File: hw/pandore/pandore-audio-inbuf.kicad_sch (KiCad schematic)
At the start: 29 parts, among them U17 OPAMP_DIFF_1

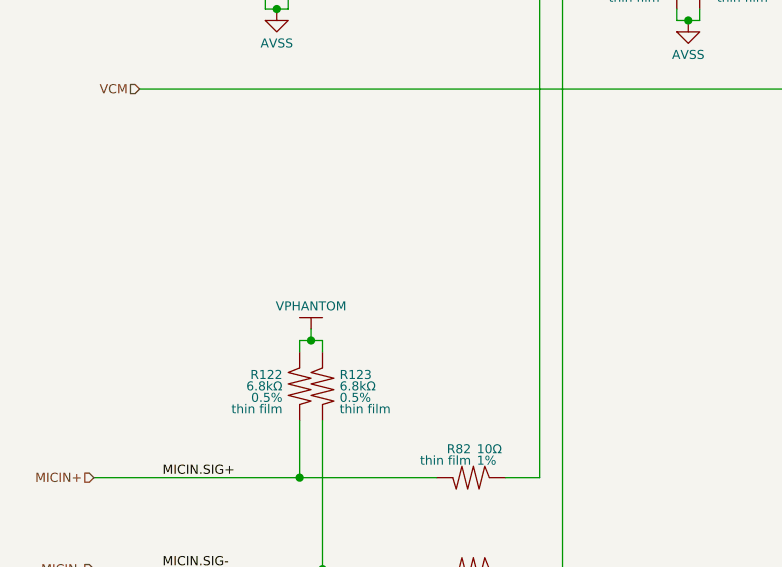
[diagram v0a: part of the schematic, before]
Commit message: Lots of routing done power blocks intra-routing mostly done rp2350 routing mostly done some label cleanup
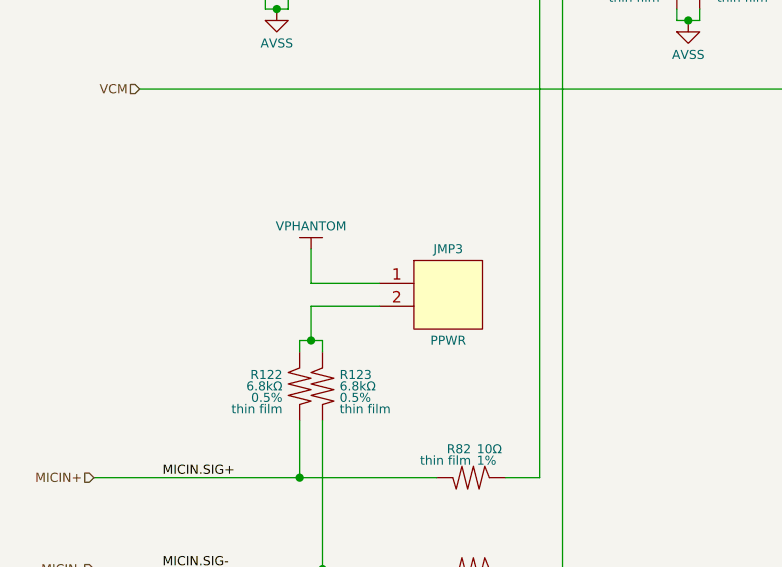
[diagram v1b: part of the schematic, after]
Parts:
- added JMP3: PPWR, reekilib_con:HDR254P1X02-TH, symbol reekilib_con:hdr-1x2
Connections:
- net VPHANTOM: now also JMP3.1; no longer R122.2, R123.2
- new net: JMP3.2, R122.2, R123.2
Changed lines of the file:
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@@
 	(wire
 		(pts
-			(xy 86.36 107.95) (xy 86.36 109.22)
-		)
-		(stroke
-			(width 0)
-			(type default)
-		)
-	)
-	(wire
-		(pts
 			(xy 156.21 77.47) (xy 156.21 62.23)
 		)
@@
 	(wire
 		(pts
+			(xy 93.98 105.41) (xy 86.36 105.41)
+		)
+		(stroke
+			(width 0)
+			(type default)
+		)
+	)
+	(wire
+		(pts
 			(xy 190.5 81.28) (xy 190.5 82.55)
 		)
@@
 	(wire
 		(pts
+			(xy 86.36 99.06) (xy 86.36 102.87)
+		)
+		(stroke
+			(width 0)
+			(type default)
+		)
+	)
+	(wire
+		(pts
 			(xy 193.04 45.72) (xy 193.04 52.07)
 		)
@@
 	(wire
 		(pts
+			(xy 86.36 102.87) (xy 93.98 102.87)
+		)
+		(stroke
+			(width 0)
+			(type default)
+		)
+	)
+	(wire
+		(pts
+			(xy 86.36 105.41) (xy 86.36 109.22)
+		)
+		(stroke
+			(width 0)
+			(type default)
+		)
+	)
+	(wire
+		(pts
 			(xy 190.5 175.26) (xy 191.77 175.26)
 		)
@@
 		)
 	)
+	(netclass_flag ""
+		(length 1.27)
+		(shape diamond)
+		(at 87.63 105.41 0)
+		(fields_autoplaced yes)
+		(effects
+			(font
+				(size 1.016 1.016)
+			)
+			(justify left bottom)
+		)
+		(property "Netclass" "PWR"
+			(at 88.7273 104.14 0)
+			(effects
+				(font
+					(size 1.27 1.27)
+				)
+				(justify left)
+			)
+		)
+		(property "Component Class" ""
+			(at -86.36 68.58 0)
+			(effects
+				(font
+					(size 1.27 1.27)
+					(italic yes)
+				)
+			)
+		)
+	)
 	(symbol
 		(lib_id "reekilib_cap:cap")
@@
 	)
 	(symbol
+		(lib_id "reekilib_con:hdr-1x2")
+		(at 101.6 104.14 0)
+		(unit 1)
+		(exclude_from_sim yes)
+		(in_bom yes)
+		(on_board yes)
+		(dnp no)
+		(fields_autoplaced yes)
+		(property "Reference" "JMP3"
+			(at 101.6 99.06 0)
+			(do_not_autoplace yes)
+			(effects
+				(font
+					(size 1 1)
+				)
+			)
+		)
+		(property "Value" "PPWR"
+			(at 101.6 109.22 0)
+			(do_not_autoplace yes)
+			(effects
+				(font
+					(size 1 1)
+				)
+			)
+		)
+		(property "Footprint" "reekilib_con:HDR254P1X02-TH"
+			(at 101.6 112.268 0)
+			(do_not_autoplace yes)
+			(effects
+				(font
+					(size 1 1)
+				)
+				(hide yes)
+			)
+		)
+		(property "Datasheet" "url-ds"
+			(at 101.6 116.586 0)
+			(do_not_autoplace yes)
+			(effects
+				(font
+					(size 1 1)
+				)
+				(hide yes)
+			)
+		)
+		(property "Description" "header 1row 2pin"
+			(at 101.6 113.792 0)
+			(do_not_autoplace yes)
+			(effects
+				(font
+					(size 1 1)
+				)
+				(hide yes)
+			)
+		)
+		(property "MPN" "MPN"
+			(at 101.6 110.744 0)
+			(do_not_autoplace yes)
+			(effects
+				(font
+					(size 1 1)
+				)
+				(hide yes)
+			)
+		)
+		(property "MFG" "MFG"
+			(at 108.204 110.744 0)
+			(do_not_autoplace yes)
+			(effects
+				(font
+					(size 1 1)
+				)
+				(justify left)
+				(hide yes)
+			)
+		)
+		(property "Link" "url-link"
+			(at 101.6 115.316 0)
+			(do_not_autoplace yes)
+			(effects
+				(font
+					(size 1 1)
+				)
+				(hide yes)
+			)
+		)
+		(pin "2"
+		)
+		(pin "1"
+		)
+		(instances
+			(project ""
+				(path "/e55f2700-f75a-4062-8a27-fe258faa8966/b4e2772d-7748-46ec-bd38-bc8e72cebcb8/505def28-a163-4964-82bd-abe7e8697de4/8d59667e-74a9-4b74-9da4-c408ef8d4019"
+					(reference "JMP3")
+					(unit 1)
+				)
+				(path "/e55f2700-f75a-4062-8a27-fe258faa8966/b4e2772d-7748-46ec-bd38-bc8e72cebcb8/505def28-a163-4964-82bd-abe7e8697de4/e109aa32-258e-4e34-aaf7-64bd999bfe07"
+					(reference "J26")
+					(unit 1)
+				)
+			)
+		)
+	)
+	(symbol
 		(lib_id "reekilib_res:res")
 		(at 127 68.58 180)
@@
 	(symbol
 		(lib_id "reekilib_pwr:VDD")
-		(at 86.36 106.68 0)
+		(at 86.36 97.79 0)
 		(unit 1)
 		(exclude_from_sim no)
@@
 		(dnp no)
 		(property "Reference" "#PWR0148"
-			(at 86.36 103.505 0)
+			(at 86.36 94.615 0)
 			(do_not_autoplace yes)
 			(effects
@@
 		)
 		(property "Value" "VPHANTOM"
-			(at 86.36 105.41 0)
+			(at 86.36 96.52 0)
 			(effects
 				(font
@@
 		)
 		(property "Footprint" ""
-			(at 86.36 106.68 0)
+			(at 86.36 97.79 0)
 			(effects
 				(font
@@
 		)
 		(property "Datasheet" ""
-			(at 86.36 106.68 0)
+			(at 86.36 97.79 0)
 			(effects
 				(font
@@
 		)
 		(property "Description" ""
-			(at 86.36 106.68 0)
+			(at 86.36 97.79 0)
 			(effects
 				(font

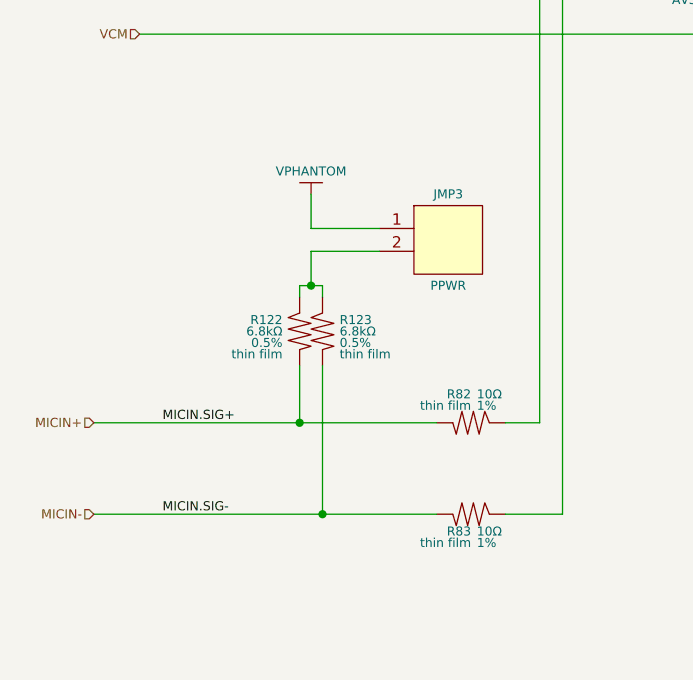
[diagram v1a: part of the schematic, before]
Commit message: lcd control circuit added fan interface added rgba output pinout for management mcu accessories done
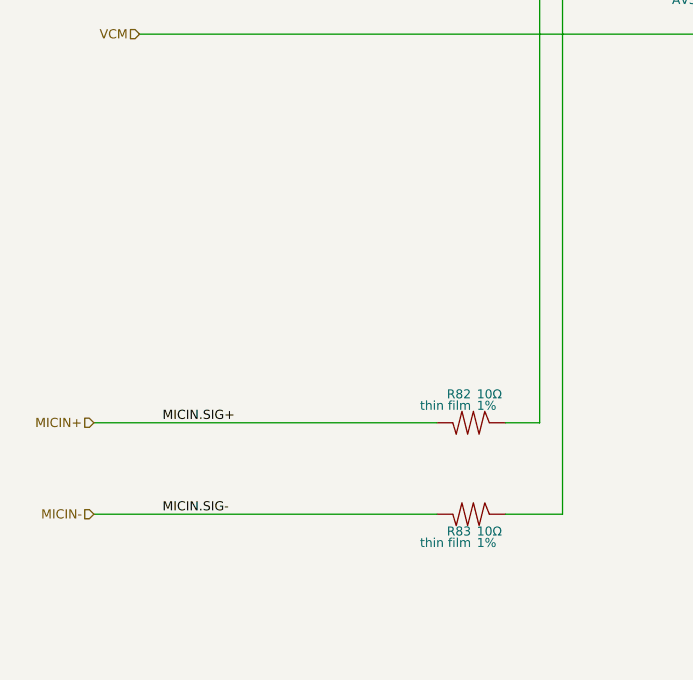
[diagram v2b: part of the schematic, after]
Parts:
- removed JMP3: PPWR, reekilib_con:HDR254P1X02-TH, symbol reekilib_con:hdr-1x2
- removed R122, R123: ${Resistance}, ${Tolerance}, ${Type}, reekilib_res:RESC2012, symbol reekilib_res:res

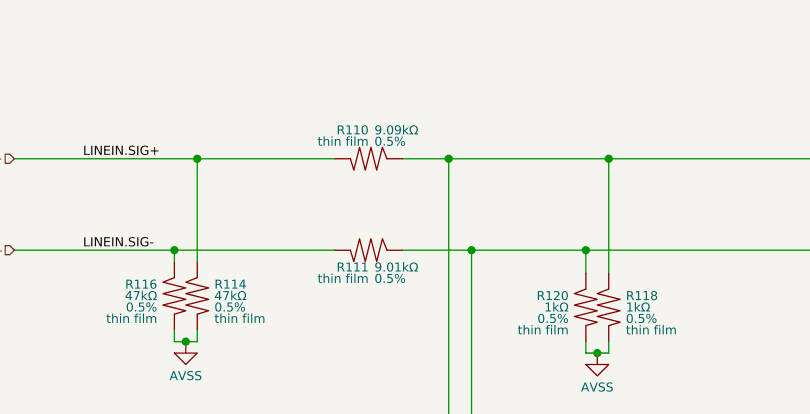
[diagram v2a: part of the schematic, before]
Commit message: added monitor amp with volume knob continue routing all around
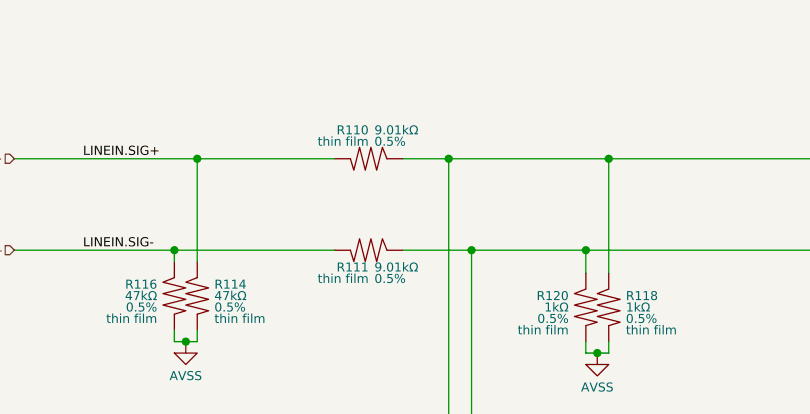
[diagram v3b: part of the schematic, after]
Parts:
- R110: Resistance 9.09kΩ -> 9.01kΩ
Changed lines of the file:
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@@
 			)
 		)
-		(property "Resistance" "9.09kΩ"
+		(property "Resistance" "9.01kΩ"
 			(at 103.505 48.895 90)
 			(do_not_autoplace yes)

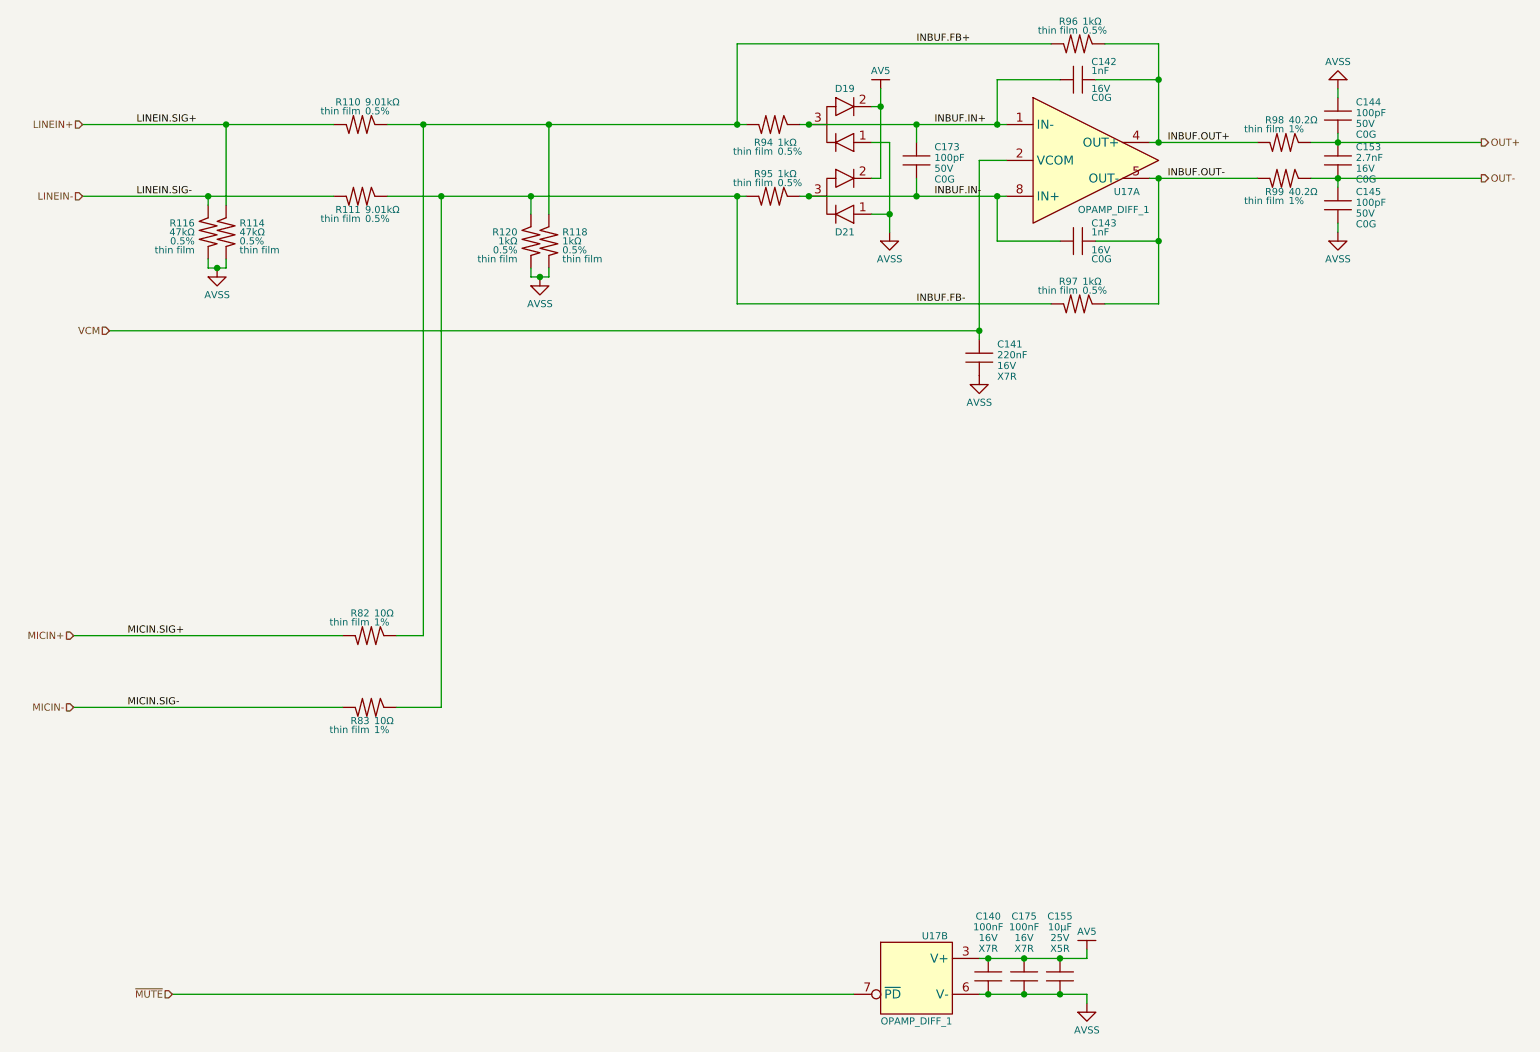
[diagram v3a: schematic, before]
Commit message: finished adding mpn,mfg to all parts, finished routing placement
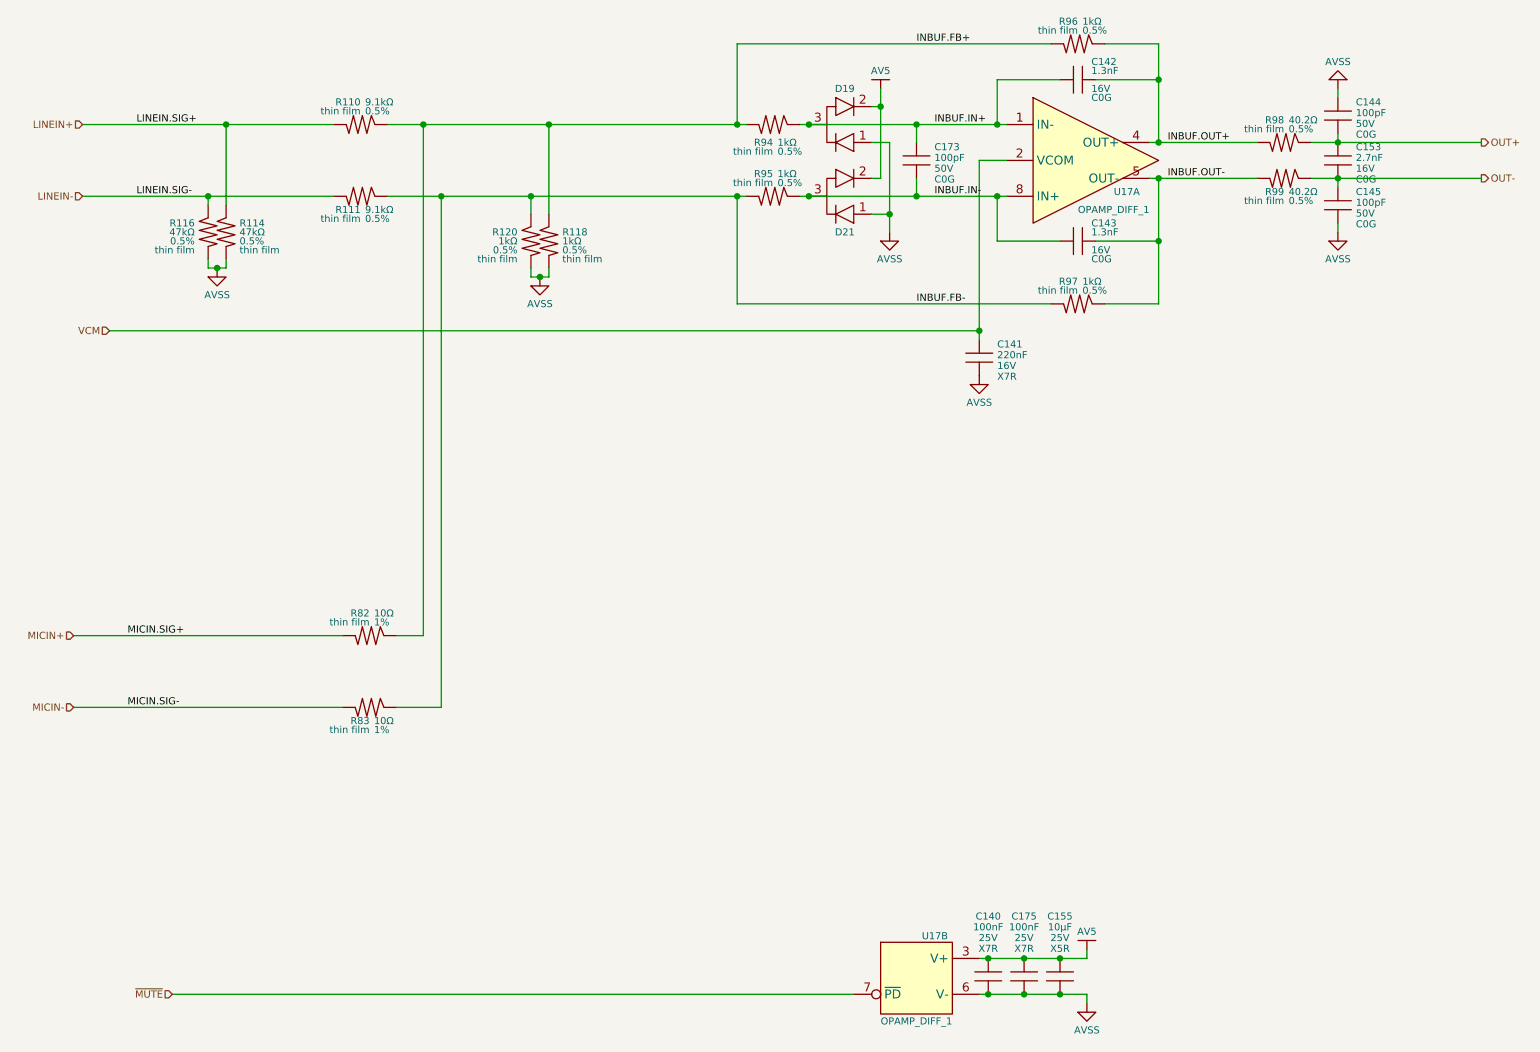
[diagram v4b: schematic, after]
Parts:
- C140, C175: MFG2 Samsung Electro-Mechanics -> (none); MFG3 Taiyo Yuden -> (none); MPN2 CL05B104KA5NNNC -> (none); MPN3 EMK105B7104KV-F -> (none); Voltage 16V -> 25V
- C141: MFG (none) -> Murata; MPN (none) -> GRM155R71C224KA12D
- C142, C143: Capacitance 1nF -> 1.3nF; MFG (none) -> Murata; MPN (none) -> GRM1885C1H132JA01D
- C144, C145, C173: MFG (none) -> Samsung Electro-Mechanics; MPN (none) -> CL10C101JB8NNNC
- C153: MFG (none) -> Murata; MPN (none) -> GCM1885C1H272JA16D
- C155: MFG (none) -> Murata; MPN (none) -> GRM21BR61E106KA73K
- R110, R111: MFG (none) -> Susumu; MPN (none) -> RR1220P-912-D; Resistance 9.01kΩ -> 9.1kΩ
- R114, R116: Link (none) -> https://yageogroup.com/products/Resistors/part/RT0805DRE074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; MFG (none) -> YAGEO; MPN (none) -> RT0805DRE0747KL
- R118, R120, R94, R95: Link (none) -> https://yageogroup.com/products/Resistors/part/RT0805DRE075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
- R82, R83: MFG (none) -> Stackpole Electronics Inc; MPN (none) -> RNCF0805DTE10R0; Power 0.25W -> 250mW
- R96, R97: Link (none) -> https://yageogroup.com/products/Resistors/part/RT0805DRE075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; MFG (none) -> YAGEO; MPN (none) -> RT0805DRE075K1L
- R98, R99: Link (none) -> https://yageogroup.com/products/Resistors/part/RT0805DRE074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; MFG (none) -> YAGEO; MPN (none) -> RT0805DRE0740R2L; Power 0.25W -> 125mW; Tolerance 1% -> 0.5%
